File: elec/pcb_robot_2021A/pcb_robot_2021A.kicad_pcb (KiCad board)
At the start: 2 copper layers, 43 parts, among them J1 LCD, J10 Encodeur 1, J11 Encodeur 2, J12 Conn_bat_power, J13 Tirette, J14 Couleur, J15 UART_backup, J16 Xbee, J17 PCA9685, J18 Capt_US, J19 I2C_backup, J2 IR 1.1, J20 lidar_in, J21 lidar_out, J22 Lidar_alim, J23 Galet 1.1, J24 Galet 1.2, J25 Galet 2.1, J26 Galet 2.2, J3 IR 1.2, J4 IR 1.3, J5 IR 2.1, J6 IR 2.2, J7 IR 2.3, J8 Moteur 1, J9 Moteur 2, U1 R-78E5.0-1.0, U2 Teensy3.5, U3 mosfet_lid_I1, U4 mosfet_lid_I2, U5 mosfet_lid_I3, U6 mosfet_lid_I4, U7 mosfet_lid_I5

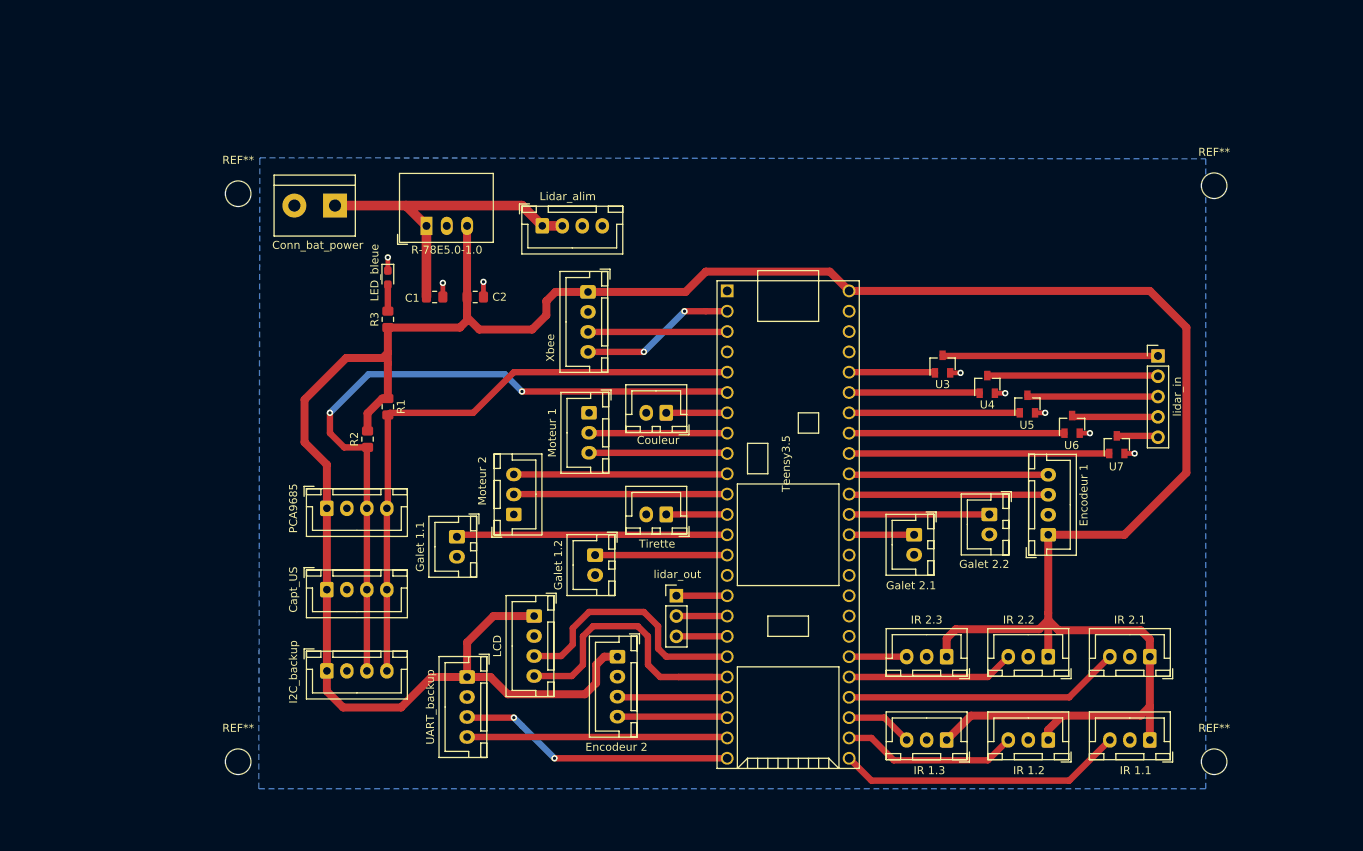
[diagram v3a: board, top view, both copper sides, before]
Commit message: Carte PCA9695 V2 : piste plus large, meilleur routage, texte au bon endroit et ajout des trous Carte Principale : Patch du texte, récupération d'une dizaine de mm sur un côté
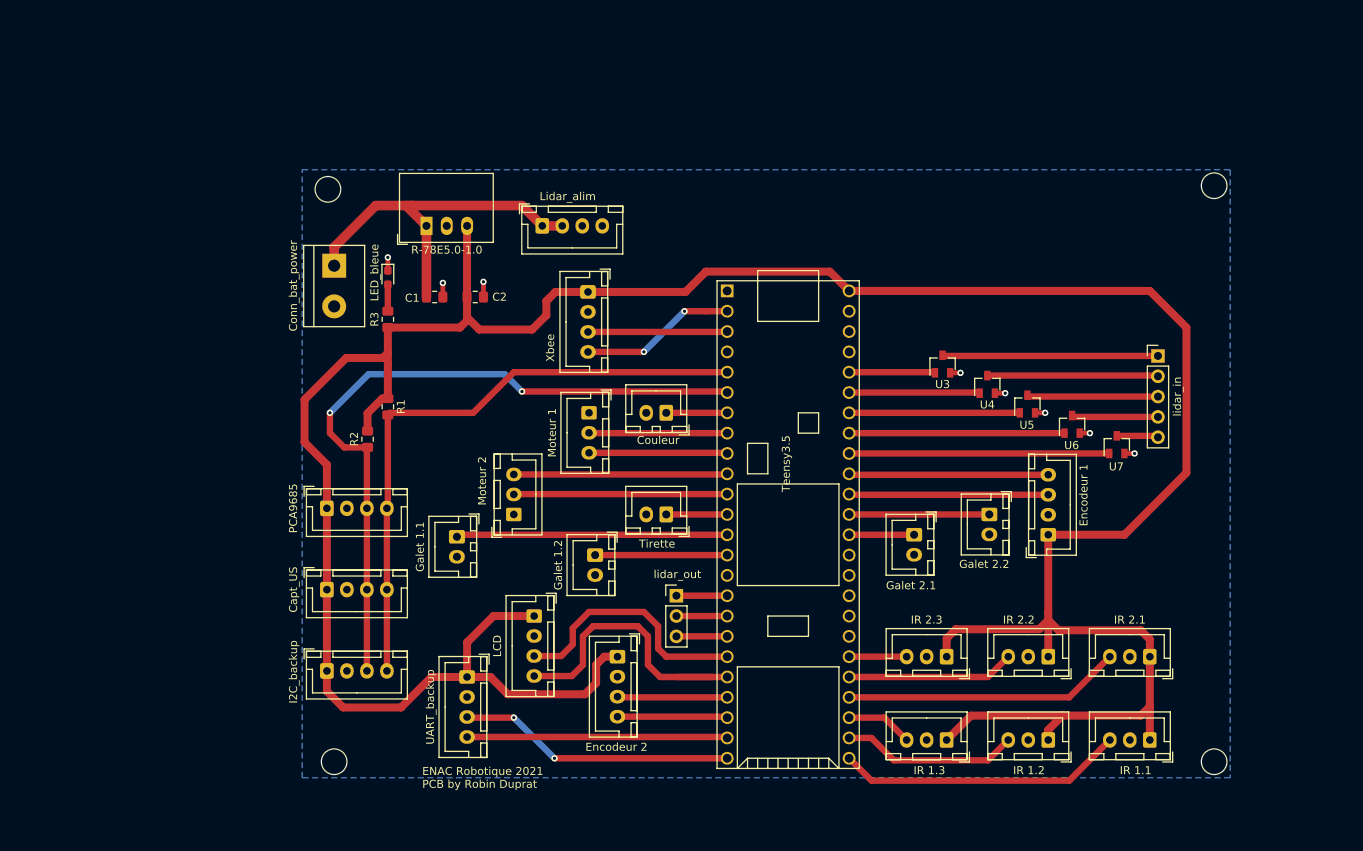
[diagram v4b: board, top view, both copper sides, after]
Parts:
- moved REF** 12.0 mm to (102.0, 116.0)
- moved REF** 11.2 mm to (101.2, 44.5)
- moved J12 7.52 mm to (102.0, 54.0), turned to 270 degrees
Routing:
- net +12V: track 41.9 -> 47.4 mm
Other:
- board text added: "ENAC Robotique 2021 PCB by Robin Duprat"
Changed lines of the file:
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@@
     (thickness 1.6)
     (drawings 9)
-    (tracks 234)
+    (tracks 237)
     (zones 0)
     (modules 43)
@@
   )
   (setup
-    (last_trace_width 1)
+    (last_trace_width 1.2)
     (user_trace_width 0.4)
     (user_trace_width 0.5)
@@
   )
   (module MountingHole:MountingHole_3.2mm_M3 (layer F.Cu)
-    (at 90 116)
+    (at 102 116)
     (descr "Mounting Hole 3.2mm, no annular, M3")
     (tags "mounting hole 3.2mm no annular m3")
     (attr virtual)
-    (fp_text reference REF** (at 0 -4.2) (layer F.SilkS)
+    (fp_text reference REF** (at 0 -4.2) (layer F.SilkS) hide
       (effects (font (size 1 1) (thickness 0.15)))
     )
@@
   )
   (module MountingHole:MountingHole_3.2mm_M3 (layer F.Cu)
-    (at 90 45)
+    (at 101.219 44.45)
     (descr "Mounting Hole 3.2mm, no annular, M3")
     (tags "mounting hole 3.2mm no annular m3")
     (attr virtual)
-    (fp_text reference REF** (at 0 -4.2) (layer F.SilkS)
+    (fp_text reference REF** (at 0 -4.2) (layer F.SilkS) hide
       (effects (font (size 1 1) (thickness 0.15)))
     )
@@
       (effects (font (size 1 1) (thickness 0.15)))
     )
-    (fp_text user %R (at 0.3 0) (layer F.Fab)
+    (fp_text user %R (at 0.3 0) (layer F.Fab) hide
       (effects (font (size 1 1) (thickness 0.15)))
     )
@@
     (tags "mounting hole 3.2mm no annular m3")
     (attr virtual)
-    (fp_text reference REF** (at 0 -4.2) (layer F.SilkS)
+    (fp_text reference REF** (at 0 -4.2) (layer F.SilkS) hide
       (effects (font (size 1 1) (thickness 0.15)))
     )
@@
     (tags "mounting hole 3.2mm no annular m3")
     (attr virtual)
-    (fp_text reference REF** (at 0 -4.2) (layer F.SilkS)
+    (fp_text reference REF** (at 0 -4.2) (layer F.SilkS) hide
       (effects (font (size 1 1) (thickness 0.15)))
     )
@@
   )
   (module TerminalBlock:TerminalBlock_bornier-2_P5.08mm (layer F.Cu)
-    (at 102.108 46.482 180)
+    (at 102 54 270)
     (descr "simple 2-pin terminal block, pitch 5.08mm, revamped version of bornier2")
     (tags "terminal block bornier2")
-    (fp_text reference J12 (at 2.54 -5.08) (layer F.SilkS) hide
-      (effects (font (size 1 1) (thickness 0.15)))
-    )
-    (fp_text value Conn_bat_power (at 2.159 -4.953) (layer F.SilkS)
+    (fp_text reference J12 (at 2.54 -5.08 90) (layer F.SilkS) hide
+      (effects (font (size 1 1) (thickness 0.15)))
+    )
+    (fp_text value Conn_bat_power (at 2.518 5.108 90) (layer F.SilkS)
       (effects (font (size 1 1) (thickness 0.15)))
     )
@@
     (fp_line (start 7.79 4) (end 7.79 -4) (layer F.CrtYd) (width 0.05))
     (fp_line (start 7.79 4) (end -2.71 4) (layer F.CrtYd) (width 0.05))
-    (pad 2 thru_hole circle (at 5.08 0 180) (size 3 3) (drill 1.52) (layers *.Cu *.Mask)
-      (net 1 GND))
-    (pad 1 thru_hole rect (at 0 0 180) (size 3 3) (drill 1.52) (layers *.Cu *.Mask)
+    (pad 2 thru_hole circle (at 5.08 0 270) (size 3 3) (drill 1.52) (layers *.Cu *.Mask)
+      (net 1 GND))
+    (pad 1 thru_hole rect (at 0 0 270) (size 3 3) (drill 1.52) (layers *.Cu *.Mask)
       (net 2 +12V))
     (model ${KISYS3DMOD}/TerminalBlock.3dshapes/TerminalBlock_bornier-2_P5.08mm.wrl
@@
     )
   )
+  (gr_line (start 96 120) (end 216 120) (layer Dwgs.User) (width 0.15))
+  (gr_line (start 98 40) (end 96 40) (layer Dwgs.User) (width 0.15))
+  (gr_line (start 96 40) (end 96 120) (layer Dwgs.User) (width 0.15))
+  (gr_text "ENAC Robotique 2021\nPCB by Robin Duprat" (at 113 118) (layer F.SilkS)
+    (effects (font (size 1 1) (thickness 0.15)) (justify left))
+  )
   (gr_line (start 216 40) (end 98 40) (layer Dwgs.User) (width 0.15))
   (gr_line (start 216 120) (end 216 40) (layer Dwgs.User) (width 0.15))
   (gr_line (start 206 120) (end 216 120) (layer Dwgs.User) (width 0.15))
-  (gr_line (start 86 120) (end 206 120) (layer Dwgs.User) (width 0.15))
-  (gr_line (start 86 45) (end 86 120) (layer Dwgs.User) (width 0.15))
-  (gr_line (start 86 40) (end 98 40) (layer Dwgs.User) (width 0.15))
-  (gr_line (start 86 45) (end 86 40) (layer Dwgs.User) (width 0.15))
   (gr_text "Robot 2021 A\nCarte principale" (at 156.972 42.926) (layer Dwgs.User)
     (effects (font (size 1 1) (thickness 0.15)))
@@
   (via (at 108.712 52.959) (size 0.8) (drill 0.4) (layers F.Cu B.Cu) (net 1))
   (segment (start 110.998 46.482) (end 113.538 49.022) (width 1.2) (layer F.Cu) (net 2))
-  (segment (start 102.108 46.482) (end 110.998 46.482) (width 1.2) (layer F.Cu) (net 2))
   (segment (start 113.538 49.022) (end 113.538 57.912) (width 1.2) (layer F.Cu) (net 2))
   (segment (start 125.476 46.482) (end 128.016 49.022) (width 1.2) (layer F.Cu) (net 2))
-  (segment (start 110.998 46.482) (end 125.476 46.482) (width 1.2) (layer F.Cu) (net 2))
   (segment (start 128.016 49.022) (end 130.516 49.022) (width 1.2) (layer F.Cu) (net 2))
+  (segment (start 111.887 46.482) (end 125.476 46.482) (width 1.2) (layer F.Cu) (net 2))
+  (segment (start 110.998 46.482) (end 111.887 46.482) (width 1.2) (layer F.Cu) (net 2))
+  (segment (start 102 54) (end 102 51.67) (width 1.2) (layer F.Cu) (net 2))
+  (segment (start 107.188 46.482) (end 111.887 46.482) (width 1.2) (layer F.Cu) (net 2))
+  (segment (start 102 51.67) (end 107.188 46.482) (width 1.2) (layer F.Cu) (net 2))
   (segment (start 108.712 70.612) (end 108.712 70.603) (width 0.8) (layer F.Cu) (net 3))
   (segment (start 101.092 84.328) (end 101.092 94.488) (width 1) (layer F.Cu) (net 3))
@@
     (polygon
       (pts
-        (xy 210.947 40.64) (xy 210.947 119.38) (xy 92.583 119.38) (xy 92.71 40.64) (xy 92.71 40.513)
+        (xy 214 118) (xy 98 118) (xy 98 42) (xy 214 42)
       )
     )

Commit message: Carte Principale : 99mm de long !!!
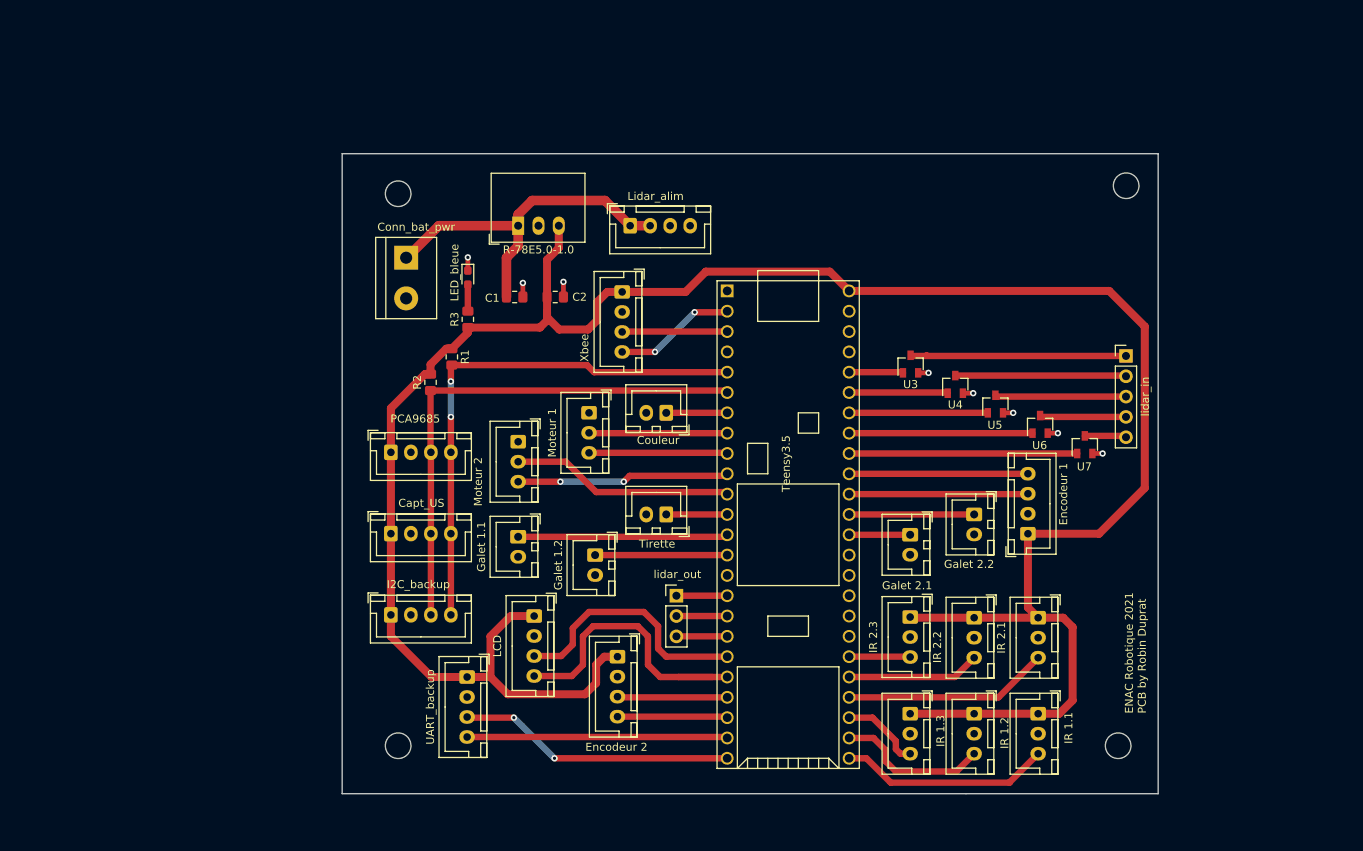
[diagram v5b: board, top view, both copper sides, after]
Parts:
- J12: value Conn_bat_power -> Conn_bat_pwr
- moved J5 14.8 mm to (190.0, 98.0), turned to 270 degrees
- moved J2 14.3 mm to (190.0, 110.0), turned to 270 degrees
- moved REF** 12.2 mm to (200.0, 114.0)
- moved U1 11.5 mm to (125.0, 49.0)
- moved REF** 11.0 mm to (201.0, 44.0)
- moved J22 11.0 mm to (139.0, 49.0)
- moved J17 10.6 mm to (109.1, 77.3)
- moved J18 10.6 mm to (109.1, 87.5)
- moved J19 10.6 mm to (109.1, 97.6)
- moved R2 10.6 mm to (114.0, 68.6)
- moved J6 10.5 mm to (182.0, 98.0), turned to 270 degrees
- moved R1 10.1 mm to (116.7, 65.4)
- moved C1 10.0 mm to (124.6, 57.9)
- moved D1 10.0 mm to (118.7, 55.5)
- moved R3 10.0 mm to (118.7, 60.7)
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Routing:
- net +5V: track 369.0 -> 294.6 mm
- net /SDA: track 88.6 -> 65.2 mm, vias 2 -> 0
- net /SCL: track 76.8 -> 66.2 mm, vias 0 -> 2
- net /IR_out1.1: track 35.9 -> 26.4 mm
- net /IR_out2.1: track 34.7 -> 25.7 mm
- net /galet_1.1: track 33.9 -> 26.2 mm
- net /IR_out2.2: track 20.9 -> 16.6 mm
- net /Xbee_RX: track 19.5 -> 15.2 mm
- net /Xbee_TX: track 17.5 -> 13.3 mm
- net /lidar_in2: track 16.4 -> 12.4 mm
- net /lidar_in5: track 32.5 -> 28.5 mm
- net /lidar_in4: track 26.9 -> 22.9 mm
- net /lidar_in3: track 21.3 -> 17.3 mm
- net /lidar_in1: track 10.8 -> 6.77 mm
- net /IR_out1.2: track 22.1 -> 19.1 mm
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- removed copper zone on B.Cu, net GND
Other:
- board outline added: 102 x 80 mm
- board text removed: "R1"

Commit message: L'alignement des trous, c'est important
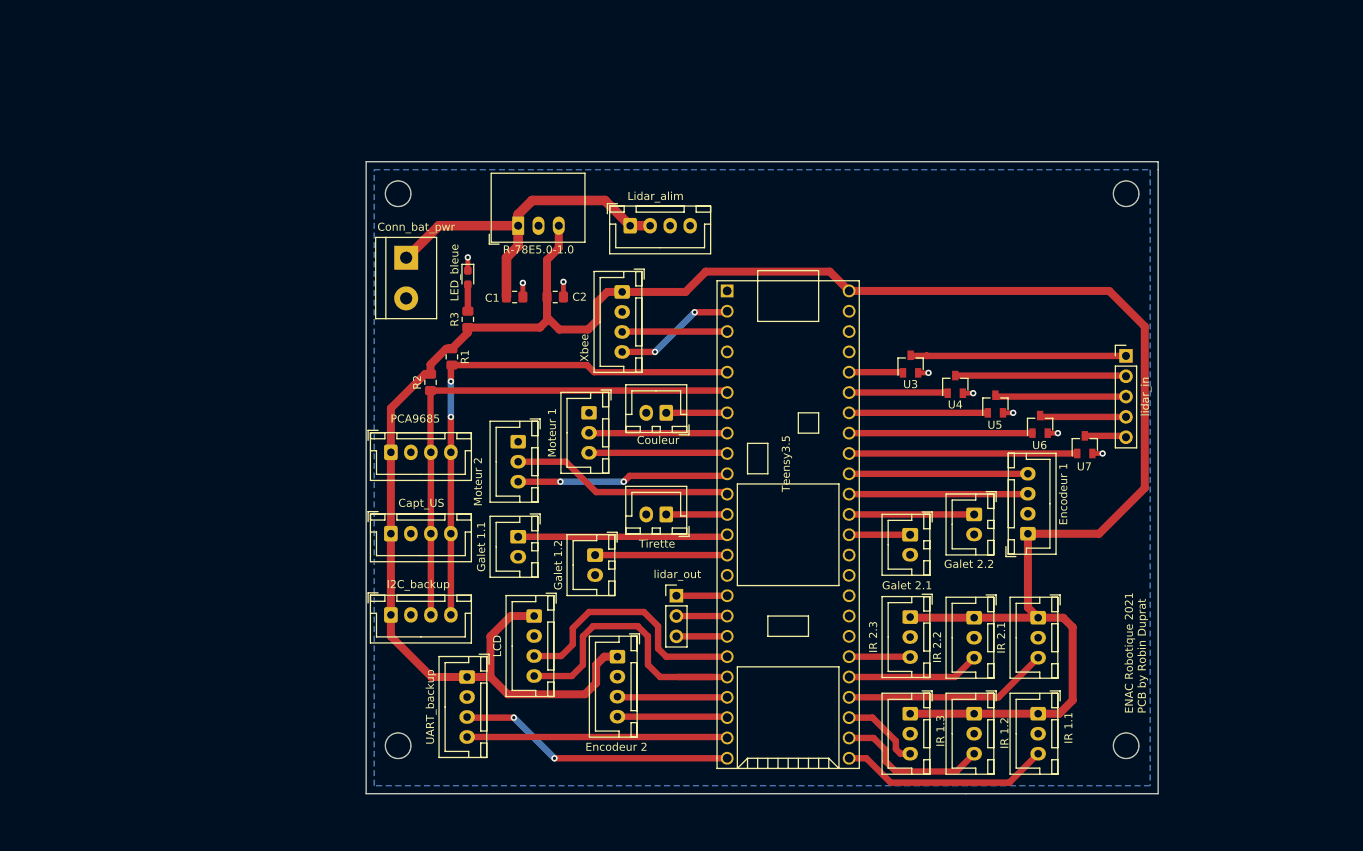
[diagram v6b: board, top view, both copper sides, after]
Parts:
- moved REF** 1.00 mm to (201.0, 45.0)
- moved REF** 1.00 mm to (201.0, 114.0)
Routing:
- added copper zone on B.Cu, net GND
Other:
- board size 102 x 80 mm -> 99 x 79 mm
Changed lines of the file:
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@@
   (general
     (thickness 1.6)
-    (drawings 7)
+    (drawings 10)
     (tracks 238)
     (zones 0)
@@
   )
   (module MountingHole:MountingHole_3.2mm_M3 (layer F.Cu)
-    (at 201 44)
+    (at 201 45)
     (descr "Mounting Hole 3.2mm, no annular, M3")
     (tags "mounting hole 3.2mm no annular m3")
@@
   )
   (module MountingHole:MountingHole_3.2mm_M3 (layer F.Cu)
-    (at 200 114)
+    (at 201 114)
     (descr "Mounting Hole 3.2mm, no annular, M3")
     (tags "mounting hole 3.2mm no annular m3")
@@
     )
   )
-  (gr_line (start 181 120) (end 103 120) (layer Edge.Cuts) (width 0.05))
-  (gr_line (start 103 40) (end 205 40) (layer Edge.Cuts) (width 0.05))
-  (gr_line (start 103 120) (end 103 40) (layer Edge.Cuts) (width 0.05))
-  (gr_line (start 205 120) (end 205 40) (layer Edge.Cuts) (width 0.05))
+  (dimension 79 (width 0.15) (layer Dwgs.User)
+    (gr_text "79,000 mm" (at 213.3 80.5 90) (layer Dwgs.User)
+      (effects (font (size 1 1) (thickness 0.15)))
+    )
+    (feature1 (pts (xy 205 41) (xy 212.586421 41)))
+    (feature2 (pts (xy 205 120) (xy 212.586421 120)))
+    (crossbar (pts (xy 212 120) (xy 212 41)))
+    (arrow1a (pts (xy 212 41) (xy 212.586421 42.126504)))
+    (arrow1b (pts (xy 212 41) (xy 211.413579 42.126504)))
+    (arrow2a (pts (xy 212 120) (xy 212.586421 118.873496)))
+    (arrow2b (pts (xy 212 120) (xy 211.413579 118.873496)))
+  )
+  (dimension 99 (width 0.15) (layer Dwgs.User)
+    (gr_text "99,000 mm" (at 155.5 125.3) (layer Dwgs.User)
+      (effects (font (size 1 1) (thickness 0.15)))
+    )
+    (feature1 (pts (xy 106 120) (xy 106 124.586421)))
+    (feature2 (pts (xy 205 120) (xy 205 124.586421)))
+    (crossbar (pts (xy 205 124) (xy 106 124)))
+    (arrow1a (pts (xy 106 124) (xy 107.126504 123.413579)))
+    (arrow1b (pts (xy 106 124) (xy 107.126504 124.586421)))
+    (arrow2a (pts (xy 205 124) (xy 203.873496 123.413579)))
+    (arrow2b (pts (xy 205 124) (xy 203.873496 124.586421)))
+  )
+  (gr_line (start 205 42) (end 205 41) (layer Edge.Cuts) (width 0.05))
+  (gr_line (start 205 120) (end 205 42) (layer Edge.Cuts) (width 0.05))
+  (gr_line (start 106 41) (end 106 120) (layer Edge.Cuts) (width 0.05))
+  (gr_line (start 205 41) (end 106 41) (layer Edge.Cuts) (width 0.05))
+  (gr_line (start 106 120) (end 181 120) (layer Edge.Cuts) (width 0.05))
   (gr_line (start 181 120) (end 205 120) (layer Edge.Cuts) (width 0.05))
   (gr_text "ENAC Robotique 2021\nPCB by Robin Duprat" (at 202.184 109.982 90) (layer F.SilkS)
@@
   (segment (start 166.37 74.93) (end 189.294 74.93) (width 0.8) (layer F.Cu) (net 47))
   (segment (start 166.37 77.47) (end 194.882 77.47) (width 0.8) (layer F.Cu) (net 48))
+  (zone (net 1) (net_name GND) (layer B.Cu) (hatch edge 0.508)
+    (connect_pads (clearance 0.508))
+    (min_thickness 0.254)
+    (fill yes (arc_segments 32) (thermal_gap 0.508) (thermal_bridge_width 0.508))
+    (polygon
+      (pts
+        (xy 204 119) (xy 107 119) (xy 107 42) (xy 204 42)
+      )
+    )
+  )
 )
